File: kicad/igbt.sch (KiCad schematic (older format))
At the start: 91 parts

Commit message: I've added LCD UI interfase, EQEP and finish ENDAT
I think I have almos all the interfases ready, I'm begining the
verigication process and then the part definig
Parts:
- removed JP?: Jumper_3_Bridged12, symbol servo:Jumper_3_Bridged12
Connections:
- wire segments 285 -> 286
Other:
- note added: "Choose a package pin-to-pin compatible with\nTI ISO7760. But SIlabs cost halt the price as TI"
- note added: "Free to other uses"
- note added: "these pins has isolation and a buffer. They could be directly connected\n to a IGBT module for test porpouses or to a power board and another\n isolation stage for production porpouses to have a reinforced isolation.\n In next stages of the development of the board, the buffers could be\n eliminated, but not the isolation Scmith trigger stage"
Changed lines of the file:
@@
 $Descr A3 16535 11693
 encoding utf-8
-Sheet 9 19
+Sheet 8 19
 Title "Igbt interface"
 Date "25 10 2019"
@@
 Wire Wire Line
 	1400 2200 1400 2100
-$Comp
-L servo:3V3H #PWR?
-U 1 1 5E190D20
-P 7550 1750
-F 0 "#PWR?" H 7550 1550 20  0001 C CNN
-F 1 "3V3H" H 7555 1907 28  0000 C CNN
-F 2 "" H 7550 1750 50  0001 C CNN
-F 3 "" H 7550 1750 50  0001 C CNN
-	1    7550 1750
-	1    0    0    -1
-$EndComp
 Text Label 10000 3400 2    50   ~ 0
 PWM_B_BRK_MEC_H
@@
 	1    0    0    -1
 $EndComp
-$Comp
-L servo:Jumper_3_Bridged12 JP?
-U 1 1 5E23B0DF
-P 7350 1750
-F 0 "JP?" H 7350 1852 50  0000 C CNN
-F 1 "Jumper_3_Bridged12" H 7350 1863 50  0001 C CNN
-F 2 "" H 7350 1750 50  0001 C CNN
-F 3 "~" H 7350 1750 50  0001 C CNN
-	1    7350 1750
-	1    0    0    -1
-$EndComp
 Wire Wire Line
 	3000 1850 4400 1850
@@
 Connection ~ 4400 1850
 Connection ~ 10300 1850
-Text Notes 4300 1100 0    197  ~ 39
+Text Notes 4300 950  0    197  ~ 39
 PWM OUT -> ISOLATOR -> BUFFER -> LED
-Wire Wire Line
-	4400 1850 7350 1850
 $Comp
 L servo:Resistor R?
@@
 Connection ~ 8650 3700
 Connection ~ 8650 3800
-Connection ~ 7350 1850
-Wire Wire Line
-	7350 1850 10300 1850
+Text Notes 700  4050 0    50   ~ 0
+Free to other uses
+Text Notes 13450 4050 0    50   ~ 0
+Free to other uses
+Text Notes 1500 4600 0    39   ~ 8
+Choose a package pin-to-pin compatible with\nTI ISO7760. But SIlabs cost halt the price as TI
+Text Notes 6600 1350 0    39   ~ 0
+these pins has isolation and a buffer. They could be directly connected\n to a IGBT module for test porpouses or to a power board and another\n isolation stage for production porpouses to have a reinforced isolation.\n In next stages of the development of the board, the buffers could be\n eliminated, but not the isolation Scmith trigger stage
+Wire Wire Line
+	4400 1850 7150 1850
+Wire Wire Line
+	7150 1750 7150 1850
+Connection ~ 7150 1850
+Wire Wire Line
+	7150 1850 10300 1850
 $EndSCHEMATC

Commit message: improve ethercat, embedded rj45 to spare, remove some unnecesary r's
I've worked on ethetcat/net to improve visibility on A3 page and also
remove some R's related to leds and change the embedded Rj45 for the
spare transformer and connector 'cause half the price and more options
to choose the connector shape and position
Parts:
- removed D? (x24): LED_A2_K1, symbol servo:LED_A2_K1
- removed J? (x2): Screw_Terminal_01x12, symbol Connector:Screw_Terminal_01x12
- removed R? (x24): 22e, symbol servo:Resistor
- added J? (x2): Screw_Terminal_01x15, symbol Connector:Screw_Terminal_01x15
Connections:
- net labels added: 15VH, FREE_OUT_A1, FREE_OUT_A2, FREE_OUT_A3, FREE_OUT_A4, FREE_OUT_B1, FREE_OUT_B2, FREE_OUT_B3, FREE_OUT_B4
- net labels removed: 3V3H
- wire segments 286 -> 297
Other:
- note added: "Free to other uses. If oyu choose another version of these IC that has\n some pins reverted to input, you could use these as an isolated general\n input also, just remember to bridge the output buffer or reverse it also"
- note added: "is an optionally 15vh out if the\n power board wanna use it"
- note removed: "Break resistor"
- note removed: "Free to other uses"
- note removed: "Mechanical break\n inside motor\n"
- moved on the sheet: R?, U?

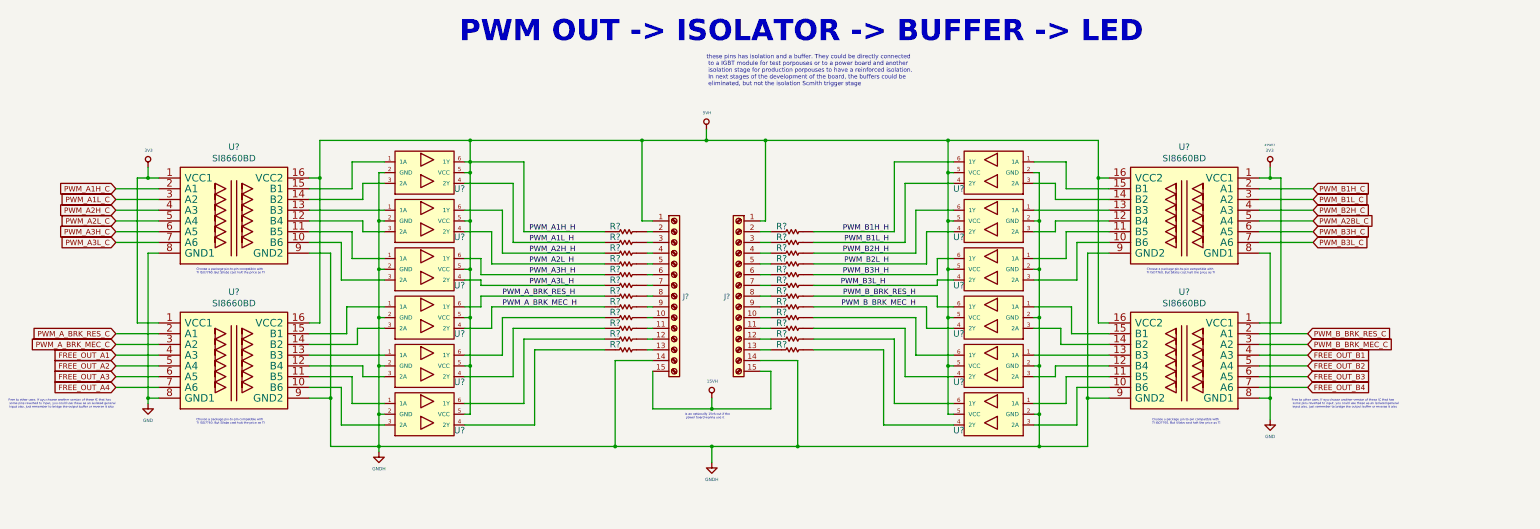
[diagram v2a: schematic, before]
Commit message: remove isolation GPIO's and replace it by free pins at IGBT
I remove completely the isolated inputs pins cause I've 8 pins free at
IGBT isolated interfase, so I leave 4 for outpus and 4 for inputs with
one isolated stage, the same as the previous isolated GPIO sheet..
I've improved the DBG sheet and some other details,. I'm ready to make
some electrical checks and fchoose the parts codes and footprints.. go
for it!
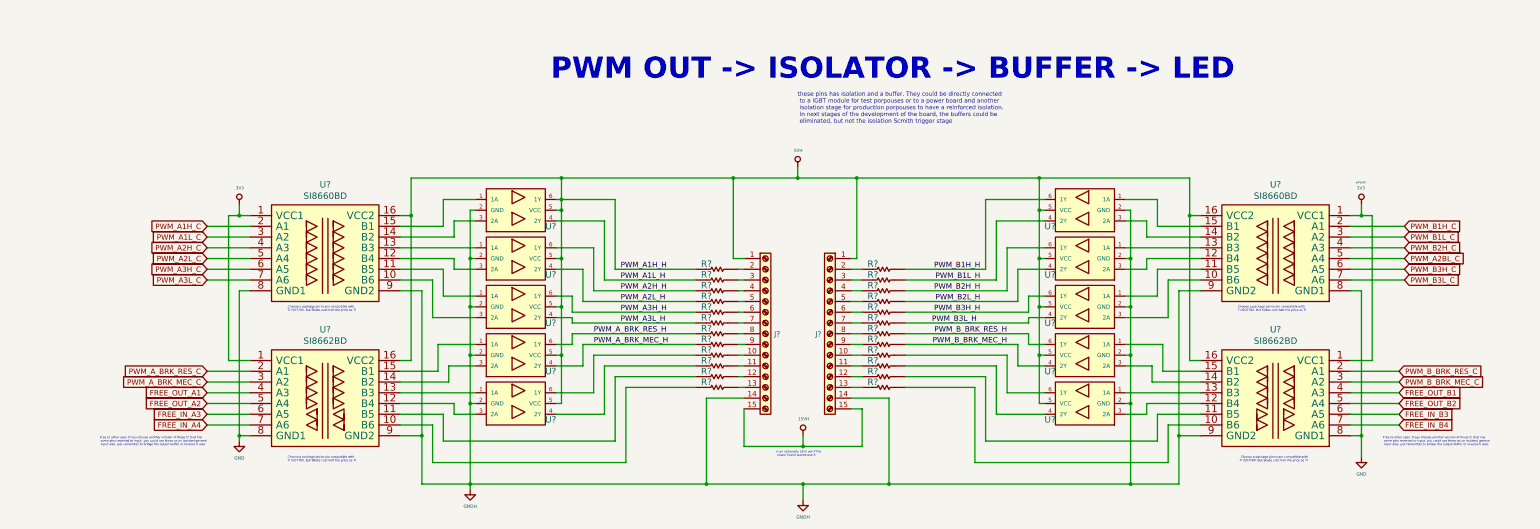
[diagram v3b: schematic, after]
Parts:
- removed U? (x2): SN74LVC2G17DBVR, symbol servo:SN74LVC2G17DBVR
- removed U? (x2): SI8660BD, symbol servo:SI8660BD
- added U? (x2): SI8662BD, symbol servo:SI8662BD
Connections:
- net 3V3: now also U?.1 (VCC1), U?.1 (VCC1)
- net 5VH: now also U?.16 (VCC2), U?.16 (VCC2)
- net FREE_OUT_A1: now also U?.4 (A3)
- net FREE_OUT_A2: now also U?.5 (A4)
- net FREE_OUT_B1: now also U?.4 (A3)
- net FREE_OUT_B2: now also U?.5 (A4)
- net GND: now also U?.8 (GND1), U?.8 (GND1)
- net GNDH: now also U?.9 (GND2), U?.9 (GND2)
- net PWM_A_BRK_MEC_C: now also U?.3 (A2)
- net PWM_A_BRK_RES_C: now also U?.2 (A1)
- net PWM_B_BRK_MEC_C: now also U?.3 (A2)
- net PWM_B_BRK_RES_C: now also U?.2 (A1)
- net at U?.1 (1A): now also U?.15 (B1) (x2)
- net at U?.3 (2A): now also U?.14 (B2) (x2)
- net at U?.1 (1A): now also U?.13 (B3) (x2)
- net at U?.3 (2A): now also U?.12 (B4) (x2)
- net at R?.1: now also U?.10 (B6)
- net at R?.1: now also U?.11 (B5)
- net at R?.2: now also U?.10 (B6)
- net at R?.2: now also U?.11 (B5)
- new net FREE_IN_A3: U?.6 (A5)
- new net FREE_IN_A4: U?.7 (A6)
- new net FREE_IN_B3: U?.6 (A5)
- new net FREE_IN_B4: U?.7 (A6)
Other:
- moved on the sheet: J?, R?, U?

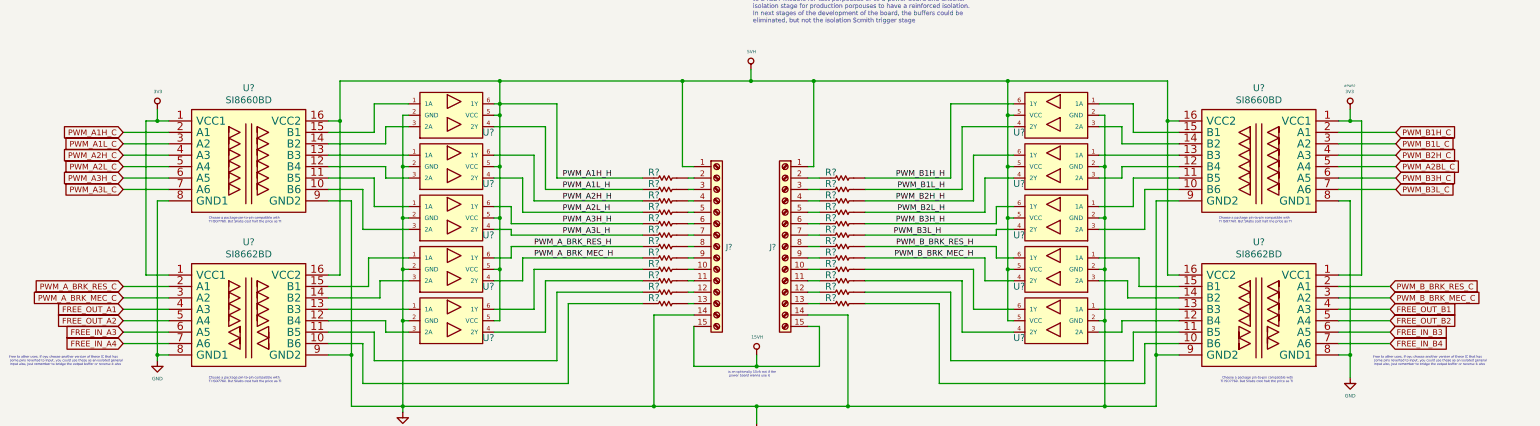
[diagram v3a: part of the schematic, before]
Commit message: added 4 push buttons and more gpios on LCD connector
just to have more UI options. With those I'd manage graphics LCD plus 4
buttons, and charaveter LCD. or the embedded EVE graphic LCD
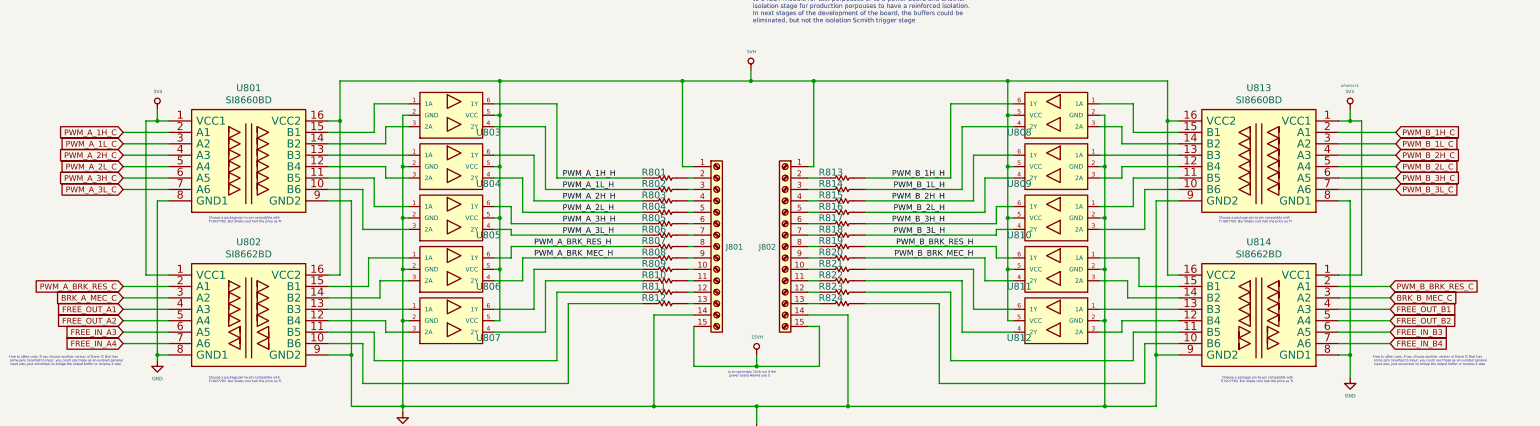
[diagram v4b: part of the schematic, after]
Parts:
- gave numbers to parts that had none: 40
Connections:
- net 5VH: no longer R801.1, U803.6 (1Y)
- net PWM_A1H_C renamed PWM_A_1H_C
- net PWM_A1L_C renamed PWM_A_1L_C
- net PWM_A1L_H renamed PWM_A_1L_H
- net PWM_A2BL_C renamed PWM_B_2L_C
- net PWM_A2H_C renamed PWM_A_2H_C
- net PWM_A2H_H renamed PWM_A_2H_H
- net PWM_A2L_C renamed PWM_A_2L_C
- net PWM_A2L_H renamed PWM_A_2L_H
- net PWM_A3H_C renamed PWM_A_3H_C
- net PWM_A3H_H renamed PWM_A_3H_H
- net PWM_A3L_C renamed PWM_A_3L_C
- net PWM_A3L_H renamed PWM_A_3L_H
- net PWM_A_BRK_MEC_C renamed BRK_A_MEC_C
- net PWM_B1H_C renamed PWM_B_1H_C
- net PWM_B1H_H renamed PWM_B_1H_H
- net PWM_B1L_C renamed PWM_B_1L_C
- net PWM_B1L_H renamed PWM_B_1L_H
- net PWM_B2H_C renamed PWM_B_2H_C
- net PWM_B2H_H renamed PWM_B_2H_H
- net PWM_B2L_H renamed PWM_B_2L_H
- net PWM_B3H_C renamed PWM_B_3H_C
- net PWM_B3H_H renamed PWM_B_3H_H
- net PWM_B3L_C renamed PWM_B_3L_C
- net PWM_B3L_H renamed PWM_B_3L_H
- net PWM_B_BRK_MEC_C renamed BRK_B_MEC_C
- new net PWM_A_1H_H: R801.1, U803.6 (1Y)

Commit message: begin PCB!! it's amess but IT IS
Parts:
- R801, R802, R803, R804, R805, R806, R807, R808, R809, R810, R811, R812, R813, R814, R815, R816, R817, R818, R819, R820, R821, R822, R823, R824: footprint (none) -> Resistor_SMD:R_0603_1608Metric
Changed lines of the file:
@@
 F 0 "R801" H 7200 3150 60  0000 C CNN
 F 1 "22e" H 7300 3203 60  0001 C CNN
-F 2 "" H 7300 3100 60  0000 C CNN
+F 2 "Resistor_SMD:R_0603_1608Metric" H 7300 3100 60  0000 C CNN
 F 3 "" H 7300 3100 60  0000 C CNN
 	1    7300 3100
@@
 F 0 "R802" H 7200 3250 60  0000 C CNN
 F 1 "22e" H 7300 3303 60  0001 C CNN
-F 2 "" H 7300 3200 60  0000 C CNN
+F 2 "Resistor_SMD:R_0603_1608Metric" H 7300 3200 60  0000 C CNN
 F 3 "" H 7300 3200 60  0000 C CNN
 	1    7300 3200
@@
 F 0 "R803" H 7200 3350 60  0000 C CNN
 F 1 "22e" H 7300 3403 60  0001 C CNN
-F 2 "" H 7300 3300 60  0000 C CNN
+F 2 "Resistor_SMD:R_0603_1608Metric" H 7300 3300 60  0000 C CNN
 F 3 "" H 7300 3300 60  0000 C CNN
 	1    7300 3300
@@
 F 0 "R804" H 7200 3450 60  0000 C CNN
 F 1 "22e" H 7300 3503 60  0001 C CNN
-F 2 "" H 7300 3400 60  0000 C CNN
+F 2 "Resistor_SMD:R_0603_1608Metric" H 7300 3400 60  0000 C CNN
 F 3 "" H 7300 3400 60  0000 C CNN
 	1    7300 3400
@@
 F 0 "R805" H 7200 3550 60  0000 C CNN
 F 1 "22e" H 7300 3603 60  0001 C CNN
-F 2 "" H 7300 3500 60  0000 C CNN
+F 2 "Resistor_SMD:R_0603_1608Metric" H 7300 3500 60  0000 C CNN
 F 3 "" H 7300 3500 60  0000 C CNN
 	1    7300 3500
@@
 F 0 "R806" H 7200 3650 60  0000 C CNN
 F 1 "22e" H 7300 3703 60  0001 C CNN
-F 2 "" H 7300 3600 60  0000 C CNN
+F 2 "Resistor_SMD:R_0603_1608Metric" H 7300 3600 60  0000 C CNN
 F 3 "" H 7300 3600 60  0000 C CNN
 	1    7300 3600
@@
 F 0 "R807" H 7200 3750 60  0000 C CNN
 F 1 "22e" H 7300 3803 60  0001 C CNN
-F 2 "" H 7300 3700 60  0000 C CNN
+F 2 "Resistor_SMD:R_0603_1608Metric" H 7300 3700 60  0000 C CNN
 F 3 "" H 7300 3700 60  0000 C CNN
 	1    7300 3700
@@
 F 0 "R808" H 7200 3850 60  0000 C CNN
 F 1 "22e" H 7300 3903 60  0001 C CNN
-F 2 "" H 7300 3800 60  0000 C CNN
+F 2 "Resistor_SMD:R_0603_1608Metric" H 7300 3800 60  0000 C CNN
 F 3 "" H 7300 3800 60  0000 C CNN
 	1    7300 3800
@@
 F 0 "R809" H 7200 3950 60  0000 C CNN
 F 1 "22e" H 7300 4003 60  0001 C CNN
-F 2 "" H 7300 3900 60  0000 C CNN
+F 2 "Resistor_SMD:R_0603_1608Metric" H 7300 3900 60  0000 C CNN
 F 3 "" H 7300 3900 60  0000 C CNN
 	1    7300 3900
@@
 F 0 "R810" H 7200 4050 60  0000 C CNN
 F 1 "22e" H 7300 4103 60  0001 C CNN
-F 2 "" H 7300 4000 60  0000 C CNN
+F 2 "Resistor_SMD:R_0603_1608Metric" H 7300 4000 60  0000 C CNN
 F 3 "" H 7300 4000 60  0000 C CNN
 	1    7300 4000
@@
 F 0 "R811" H 7200 4150 60  0000 C CNN
 F 1 "22e" H 7300 4203 60  0001 C CNN
-F 2 "" H 7300 4100 60  0000 C CNN
+F 2 "Resistor_SMD:R_0603_1608Metric" H 7300 4100 60  0000 C CNN
 F 3 "" H 7300 4100 60  0000 C CNN
 	1    7300 4100
@@
 F 0 "R812" H 7200 4250 60  0000 C CNN
 F 1 "22e" H 7300 4303 60  0001 C CNN
-F 2 "" H 7300 4200 60  0000 C CNN
+F 2 "Resistor_SMD:R_0603_1608Metric" H 7300 4200 60  0000 C CNN
 F 3 "" H 7300 4200 60  0000 C CNN
 	1    7300 4200
@@
 F 0 "R813" H 8750 3150 60  0000 C CNN
 F 1 "22e" H 8850 3203 60  0001 C CNN
-F 2 "" H 8850 3100 60  0000 C CNN
+F 2 "Resistor_SMD:R_0603_1608Metric" H 8850 3100 60  0000 C CNN
 F 3 "" H 8850 3100 60  0000 C CNN
 	1    8850 3100
@@
 F 0 "R814" H 8750 3250 60  0000 C CNN
 F 1 "22e" H 8850 3303 60  0001 C CNN
-F 2 "" H 8850 3200 60  0000 C CNN
+F 2 "Resistor_SMD:R_0603_1608Metric" H 8850 3200 60  0000 C CNN
 F 3 "" H 8850 3200 60  0000 C CNN
 	1    8850 3200
@@
 F 0 "R815" H 8750 3350 60  0000 C CNN
 F 1 "22e" H 8850 3403 60  0001 C CNN
-F 2 "" H 8850 3300 60  0000 C CNN
+F 2 "Resistor_SMD:R_0603_1608Metric" H 8850 3300 60  0000 C CNN
 F 3 "" H 8850 3300 60  0000 C CNN
 	1    8850 3300
@@
 F 0 "R816" H 8750 3450 60  0000 C CNN
 F 1 "22e" H 8850 3503 60  0001 C CNN
-F 2 "" H 8850 3400 60  0000 C CNN
+F 2 "Resistor_SMD:R_0603_1608Metric" H 8850 3400 60  0000 C CNN
 F 3 "" H 8850 3400 60  0000 C CNN
 	1    8850 3400
@@
 F 0 "R817" H 8750 3550 60  0000 C CNN
 F 1 "22e" H 8850 3603 60  0001 C CNN
-F 2 "" H 8850 3500 60  0000 C CNN
+F 2 "Resistor_SMD:R_0603_1608Metric" H 8850 3500 60  0000 C CNN
 F 3 "" H 8850 3500 60  0000 C CNN
 	1    8850 3500
@@
 F 0 "R818" H 8750 3650 60  0000 C CNN
 F 1 "22e" H 8850 3703 60  0001 C CNN
-F 2 "" H 8850 3600 60  0000 C CNN
+F 2 "Resistor_SMD:R_0603_1608Metric" H 8850 3600 60  0000 C CNN
 F 3 "" H 8850 3600 60  0000 C CNN
 	1    8850 3600
@@
 F 0 "R819" H 8750 3750 60  0000 C CNN
 F 1 "22e" H 8850 3803 60  0001 C CNN
-F 2 "" H 8850 3700 60  0000 C CNN
+F 2 "Resistor_SMD:R_0603_1608Metric" H 8850 3700 60  0000 C CNN
 F 3 "" H 8850 3700 60  0000 C CNN
 	1    8850 3700
@@
 F 0 "R820" H 8750 3850 60  0000 C CNN
 F 1 "22e" H 8850 3903 60  0001 C CNN
-F 2 "" H 8850 3800 60  0000 C CNN
+F 2 "Resistor_SMD:R_0603_1608Metric" H 8850 3800 60  0000 C CNN
 F 3 "" H 8850 3800 60  0000 C CNN
 	1    8850 3800
@@
 F 0 "R821" H 8750 3950 60  0000 C CNN
 F 1 "22e" H 8850 4003 60  0001 C CNN
-F 2 "" H 8850 3900 60  0000 C CNN
+F 2 "Resistor_SMD:R_0603_1608Metric" H 8850 3900 60  0000 C CNN
 F 3 "" H 8850 3900 60  0000 C CNN
 	1    8850 3900
@@
 F 0 "R822" H 8750 4050 60  0000 C CNN
 F 1 "22e" H 8850 4103 60  0001 C CNN
-F 2 "" H 8850 4000 60  0000 C CNN
+F 2 "Resistor_SMD:R_0603_1608Metric" H 8850 4000 60  0000 C CNN
 F 3 "" H 8850 4000 60  0000 C CNN
 	1    8850 4000
@@
 F 0 "R823" H 8750 4150 60  0000 C CNN
 F 1 "22e" H 8850 4203 60  0001 C CNN
-F 2 "" H 8850 4100 60  0000 C CNN
+F 2 "Resistor_SMD:R_0603_1608Metric" H 8850 4100 60  0000 C CNN
 F 3 "" H 8850 4100 60  0000 C CNN
 	1    8850 4100
@@
 F 0 "R824" H 8750 4250 60  0000 C CNN
 F 1 "22e" H 8850 4303 60  0001 C CNN
-F 2 "" H 8850 4200 60  0000 C CNN
+F 2 "Resistor_SMD:R_0603_1608Metric" H 8850 4200 60  0000 C CNN
 F 3 "" H 8850 4200 60  0000 C CNN
 	1    8850 4200
